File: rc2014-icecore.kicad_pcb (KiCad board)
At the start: 2 copper layers, 100 x 60.4 mm, 50 parts, among them J1 Conn_02x40_Top_Bottom, J2 Config, J3 DB15_Female_HighDensity_Mount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, P1 Mini-DIN_6pins_ver2, U1 SN74CB3T3245, U2 SN74CB3T3245, U3 SN74CB3T3245, U4 SN74CB3T3245, U5 SN74CB3T3245, U6 LM1117-3.3

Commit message: WIP
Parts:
- removed P1: Mini-DIN_6pins_ver2, 4x1md:Connector_Mini-DIN_Female_6Pin_2rows
- removed R1, R10, R11, R12, R16, R17, R18, R19, R2, R20, R24, R3, R4, R8, R9: 536, Resistor_SMD:R_0603_1608Metric
- removed R13, R14, R15, R21, R22, R23, R5, R6, R7: 270, Resistor_SMD:R_0603_1608Metric
- removed R25, R26: 100, Resistor_SMD:R_0603_1608Metric
- added J4: Conn_02x15_Odd_Even, Connector_PinSocket_2.54mm:PinSocket_2x15_P2.54mm_Horizontal, F.Cu at (128.3, 101.1)
- added J5: Conn_02x13_Odd_Even, Connector_PinHeader_2.54mm:PinHeader_2x13_P2.54mm_Horizontal, F.Cu at (266.1, 69.6)
- J3: value DB15_Female_HighDensity_MountingHoles -> Conn_02x15_Odd_Even; footprint Connector_Dsub:DSUB-15-HD_Female_Horizontal_P2.29x1.98mm_EdgePinOffset3.03mm_Housed_MountingHolesOffset4.94mm -> Connector_PinSocket_2.54mm:PinSocket_2x15_P2.54mm_Horizontal
- moved C11 24.7 mm to (127.1, 123.5)
- moved C7 24.7 mm to (123.3, 128.0)
- moved C6 24.7 mm to (127.3, 117.1)
- moved C12 24.7 mm to (131.4, 128.0)
- moved J3 16.8 mm to (140.9, 148.1), turned to 180 degrees
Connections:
- A1 pad 17: /VGA_R0 -> (no net)
- A1 pad 18: /VGA_R1 -> (no net)
- A1 pad 19: /VGA_R2 -> (no net)
- A1 pad 20: /VGA_G0 -> (no net)
- A1 pad 21: /VGA_G1 -> (no net)
- A1 pad 22: /VGA_G2 -> (no net)
- A1 pad 23: /VGA_B0 -> (no net)
- A1 pad 24: /VGA_B1 -> (no net)
- A1 pad 42: /VGA_HS -> (no net)
- A1 pad 43: /VGA_VS -> (no net)
- A1 pad 44: /VGA_B2 -> (no net)
- A1 pad 97: (no net) -> /RC_OE
- J2 pad 11: /DATA_OE -> (no net)
- J2 pad 13: /SIG_OE -> (no net)
- J2 pad 15: /SIG2_OE -> (no net)
- J2 pad 9: /ADDR_OE -> (no net)
- J3 pad 1: Net-(J3-Pad1) -> (no net)
- J3 pad 10: GND -> (no net)
- J3 pad 13: Net-(J3-Pad13) -> (no net)
- J3 pad 14: Net-(J3-Pad14) -> (no net)
- J3 pad 2: Net-(J3-Pad2) -> (no net)
- J3 pad 3: Net-(J3-Pad3) -> (no net)
- J3 pad 5: GND -> (no net)
- J3 pad 6: GND -> (no net)
- J3 pad 7: GND -> (no net)
- J3 pad 8: GND -> (no net)
- U1 pad 19: /ADDR_OE -> /RC_OE
- U2 pad 19: /ADDR_OE -> /RC_OE
- U3 pad 19: /SIG_OE -> /RC_OE
- U4 pad 19: /SIG2_OE -> /RC_OE
- U5 pad 19: /DATA_OE -> /RC_OE
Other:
- board size 100 x 60.4 mm -> 100.1 x 70.1 mm

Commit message: Board routed
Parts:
- removed C10, C11, C12, C8, C9: C, Capacitor_SMD:C_0603_1608Metric
- removed J2: Config, Connector_PinHeader_2.54mm:PinHeader_2x08_P2.54mm_Vertical
- removed J4: Conn_02x15_Odd_Even, Connector_PinSocket_2.54mm:PinSocket_2x15_P2.54mm_Horizontal
- moved J5 217.6 mm to (64.5, 151.6), turned to 180 degrees
- moved C2 77.8 mm to (149.5, 142.4)
- moved U6 77.8 mm to (143.1, 145.5)
- moved JP1 73.7 mm to (143.5, 129.7)
- moved C1 71.5 mm to (136.4, 142.2)
- moved C3 28.6 mm to (82.5, 120.4)
- moved C5 24.3 mm to (104.6, 120.4)
- moved C4 21.5 mm to (93.7, 120.4)
- moved J3 15.6 mm to (156.5, 147.3)
- moved U1 12.2 mm to (85.6, 127.5)
- moved U2 12.2 mm to (96.8, 127.5)
- moved U3 12.2 mm to (107.7, 127.5)
- moved U4 12.2 mm to (119.4, 127.5)
- moved U5 12.2 mm to (130.9, 127.5)
- moved C6 11.3 mm to (116.6, 120.7)
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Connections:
- A1 pad 1: /A14LV -> /P0
- A1 pad 10: /CLKLV -> /P17
- A1 pad 100: (no net) -> /P55
- A1 pad 11: /MREQLV -> /P20
- A1 pad 12: //RDLV -> /P21
- A1 pad 13: /D0LV -> /P24
- A1 pad 14: /D2LV -> /P25
- A1 pad 15: /D4LV -> /P28
- A1 pad 16: /D6LV -> /P29
- A1 pad 17: (no net) -> /P32
- A1 pad 18: (no net) -> /P33
- A1 pad 19: (no net) -> /P36
- A1 pad 2: /A12LV -> /P1
- A1 pad 20: (no net) -> /P37
- A1 pad 21: (no net) -> /P40
- A1 pad 22: (no net) -> /P41
- A1 pad 23: (no net) -> /P44
- A1 pad 24: (no net) -> /P45
- A1 pad 26: /A15LV -> /P2
- A1 pad 27: /A13LV -> /P3
- A1 pad 28: /A11LV -> /P6
- A1 pad 29: /A9LV -> /P7
- A1 pad 3: /A10LV -> /P4
- A1 pad 30: /A7LV -> /P10
- A1 pad 31: /A5LV -> /P11
- A1 pad 32: /A3LV -> /P14
- A1 pad 33: /A1LV -> /P15
- A1 pad 34: //RESETLV -> /P18
- A1 pad 35: /INTLV -> /P19
- A1 pad 36: //WRLV -> /P22
- A1 pad 37: //IORQLV -> /P23
- A1 pad 38: /D1LV -> /P26
- A1 pad 39: /D3LV -> /P27
- A1 pad 4: /A8LV -> /P5
- A1 pad 40: /D5LV -> /P30
- A1 pad 41: /D7LV -> /P31
- A1 pad 42: (no net) -> /P34
- A1 pad 43: (no net) -> /P35
- A1 pad 44: (no net) -> /P38
- A1 pad 45: (no net) -> /P39
- A1 pad 46: (no net) -> /P42
- A1 pad 47: (no net) -> /P43
- A1 pad 48: (no net) -> /P46
- A1 pad 49: (no net) -> /P47
- A1 pad 5: /A6LV -> /P8
- A1 pad 50: (no net) -> /FPGA_VCC
- A1 pad 52: (no net) -> /SWDIO
- A1 pad 53: (no net) -> /SWCLK
- A1 pad 54: (no net) -> /~RESET
- A1 pad 6: /A4LV -> /P9
- A1 pad 60: (no net) -> /AN5
- A1 pad 61: (no net) -> /AN6
- A1 pad 62: (no net) -> /AN7
- A1 pad 63: (no net) -> /AN8
- A1 pad 64: (no net) -> /AN9
- A1 pad 7: /A2LV -> /P12
- A1 pad 76: (no net) -> GND
- A1 pad 77: (no net) -> /~ESS
- A1 pad 78: (no net) -> /TX
- A1 pad 79: (no net) -> /RX
- A1 pad 8: /A0LV -> /P13
- A1 pad 80: (no net) -> /ESCK
- A1 pad 81: (no net) -> /EMISO
- A1 pad 82: (no net) -> /EMOSI
- A1 pad 83: (no net) -> /SCL
- A1 pad 84: (no net) -> /SDA
- A1 pad 85: (no net) -> /TMS
- A1 pad 86: (no net) -> /TDO
- A1 pad 87: (no net) -> /TDI
- A1 pad 88: (no net) -> /TCK
- A1 pad 89: (no net) -> +5V
- A1 pad 9: /M1LV -> /P16
- A1 pad 93: (no net) -> /P48
- A1 pad 94: (no net) -> /P49
- A1 pad 95: (no net) -> /P50
- A1 pad 96: (no net) -> /P51
- A1 pad 97: /RC_OE -> /P52
- A1 pad 98: (no net) -> /P53
- A1 pad 99: (no net) -> /P54
- J1 pad 33: (no net) -> GND
- J1 pad 38: (no net) -> /~RFSH
- J1 pad 44: (no net) -> /BUSACK
- J1 pad 46: (no net) -> /~HALT
- J1 pad 50: (no net) -> /~WAIT
- J1 pad 52: (no net) -> /~NMI
- J3 pad 1: (no net) -> +3V3
- J3 pad 10: (no net) -> /P36
- J3 pad 11: (no net) -> /P39
- J3 pad 12: (no net) -> /P37
- J3 pad 13: (no net) -> /AN9
- J3 pad 14: (no net) -> /AN8
- J3 pad 15: (no net) -> +5V
- J3 pad 16: (no net) -> /AN7
- J3 pad 17: (no net) -> /AN6
- J3 pad 18: (no net) -> /AN5
- J3 pad 19: (no net) -> +3V3
- J3 pad 2: (no net) -> +3V3
- J3 pad 20: (no net) -> +3V3
- J3 pad 21: (no net) -> GND
- J3 pad 22: (no net) -> GND
- J3 pad 23: (no net) -> /P42
- J3 pad 24: (no net) -> /P46
- J3 pad 25: (no net) -> /P43
- J3 pad 26: (no net) -> /P47
- J3 pad 27: (no net) -> /P40
- J3 pad 28: (no net) -> /P44
- J3 pad 29: (no net) -> /P41
- J3 pad 3: (no net) -> GND
- J3 pad 30: (no net) -> /P45
- J3 pad 4: (no net) -> GND
- J3 pad 5: (no net) -> /P34
- J3 pad 6: (no net) -> /P32
- J3 pad 7: (no net) -> /P35
- J3 pad 8: (no net) -> /P33
- J3 pad 9: (no net) -> /P38
- J5 pad 10: (no net) -> /TX
- J5 pad 11: (no net) -> /SWDIO
- J5 pad 12: (no net) -> /TCK
- J5 pad 13: (no net) -> /~RESET
- J5 pad 14: (no net) -> GND
- J5 pad 15: (no net) -> /TMS
- J5 pad 16: (no net) -> /TDI
- J5 pad 18: (no net) -> /TDO
- J5 pad 19: (no net) -> /EMOSI
- J5 pad 2: (no net) -> Net-(J5-Pad2)
- J5 pad 20: (no net) -> GND
- J5 pad 21: (no net) -> /EMISO
- J5 pad 23: (no net) -> /ESCK
- J5 pad 24: (no net) -> /~ESS
- J5 pad 25: (no net) -> GND
- J5 pad 3: (no net) -> /SDA
- J5 pad 4: (no net) -> Net-(J5-Pad2)
- J5 pad 5: (no net) -> /SCL
- J5 pad 6: (no net) -> GND
- J5 pad 7: (no net) -> /SWCLK
- J5 pad 8: (no net) -> /RX
- J5 pad 9: (no net) -> GND
- JP1 pad 3: (no net) -> /FPGA_VCC
- U1 pad 11: /A8LV -> /P8
- U1 pad 12: /A9LV -> /P6
- U1 pad 13: /A10LV -> /P5
- U1 pad 14: /A11LV -> /P3
- U1 pad 15: /A12LV -> /P4
- U1 pad 16: /A13LV -> /P2
- U1 pad 17: /A14LV -> /P1
- U1 pad 18: /A15LV -> /P0
- U1 pad 19: /RC_OE -> /P23
- U2 pad 11: /A0LV -> /P15
- U2 pad 12: /A1LV -> /P14
- U2 pad 13: /A2LV -> /P13
- U2 pad 14: /A3LV -> /P11
- U2 pad 15: /A4LV -> /P12
- U2 pad 16: /A5LV -> /P10
- U2 pad 17: /A6LV -> /P9
- U2 pad 18: /A7LV -> /P7
- U2 pad 19: /RC_OE -> /P23
- U3 pad 11: //IORQLV -> /P21
- U3 pad 12: //RDLV -> /P22
- U3 pad 13: //WRLV -> /P20
- U3 pad 14: /MREQLV -> /P19
- U3 pad 15: /M1LV -> /P17
- U3 pad 16: (no net) -> /P18
- U3 pad 17: (no net) -> /P16
- U3 pad 19: /RC_OE -> /P23
- U3 pad 4: (no net) -> /M1
- U3 pad 5: /M1 -> /~RFSH
- U3 pad 6: /MREQ -> //RESET
- U3 pad 7: //WR -> /CLK
- U3 pad 8: //RD -> /INT
- U3 pad 9: //IORQ -> /BUSACK
- U4 pad 11: /INTLV -> /P31
- U4 pad 12: /CLKLV -> /P29
- U4 pad 13: //RESETLV -> /P30
- U4 pad 14: (no net) -> /P28
- U4 pad 15: (no net) -> /P27
- U4 pad 16: (no net) -> /P25
- U4 pad 17: (no net) -> /P26
- U4 pad 18: (no net) -> /P24
- U4 pad 19: /RC_OE -> /P23
- U4 pad 2: (no net) -> /MREQ
- U4 pad 3: (no net) -> /~HALT
- U4 pad 4: (no net) -> //WR
- U4 pad 6: (no net) -> //RD
- U4 pad 7: //RESET -> /~WAIT
- U4 pad 8: /CLK -> //IORQ
- U4 pad 9: /INT -> /~NMI
- U5 pad 11: /D7LV -> /P55
- U5 pad 12: /D6LV -> /P54
- U5 pad 13: /D5LV -> /P53
- U5 pad 14: /D4LV -> /P52
- U5 pad 15: /D3LV -> /P51
- U5 pad 16: /D2LV -> /P50
- U5 pad 17: /D1LV -> /P49
- U5 pad 18: /D0LV -> /P48
- U5 pad 19: /RC_OE -> /P23
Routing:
- net GND: track 0.00 -> 191.8 mm, vias 0 -> 13
- net +3V3: track 0.00 -> 131.5 mm, vias 0 -> 6
- net +5V: track 0.00 -> 80.2 mm, vias 0 -> 2
- net /AN5: track 0.00 -> 74.7 mm, vias 0 -> 1
- net /P23: track 0.00 -> 70.2 mm
- net /AN6: track 0.00 -> 70.1 mm, vias 0 -> 1
- net /AN7: track 0.00 -> 66.7 mm, vias 0 -> 1
- net /P32: track 0.00 -> 64.5 mm
- net /AN8: track 0.00 -> 63.7 mm, vias 0 -> 2
- net /P33: track 0.00 -> 61.6 mm
- net /P36: track 0.00 -> 59.0 mm
- net /P34: track 0.00 -> 58.3 mm
- net /AN9: track 0.00 -> 56.8 mm, vias 0 -> 2
- net /P37: track 0.00 -> 56.7 mm
- net /TCK: track 0.00 -> 56.1 mm, vias 0 -> 1
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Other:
- board size 100.1 x 70.1 mm -> 100.1 x 63.3 mm
- net class Default: clearance 0.2 -> 0.1524
- net class gnd removed
- rule trace_clearance: 0.2 -> 0.1524
- board text added: "RC2014 IceCore Interface"
- board text removed: "RC2014 5V <-> 3.3V FPGA Interface"

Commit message: Board redesign
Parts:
- added J2: Conn_01x10, rc2014:PinHeader_1x10_P2.54mm_Vertical_NoSilk, F.Cu at (102.4, 160.8)
- J1: value Conn_02x40_Top_Bottom -> Conn_01x39; footprint Connector_PinHeader_2.54mm:PinHeader_2x39_P2.54mm_Vertical -> rc2014:PinHeader_1x39_P2.54mm_Vertical_NoSilk
- moved JP1 71.9 mm to (71.8, 124.6)
- moved C2 50.9 mm to (99.6, 132.2), turned to 180 degrees
- moved U1 43.4 mm to (100.3, 138.2)
- moved C1 41.3 mm to (95.6, 135.8), turned to 270 degrees
- moved J3 29.7 mm to (126.7, 146.6)
- moved C3 22.3 mm to (115.6, 139.2), turned to 270 degrees
- moved U6 17.5 mm to (120.5, 141.6)
- moved A1 8.52 mm to (84.7, 105.9)
- moved C7 6.70 mm to (110.7, 124.0), turned to 270 degrees
- moved C5 6.62 mm to (88.1, 124.0), turned to 270 degrees
- moved C4 6.41 mm to (77.2, 124.0), turned to 270 degrees
- moved C6 6.10 mm to (99.7, 124.0), turned to 270 degrees
- moved U5 4.10 mm to (115.6, 126.0)
- moved U3 3.87 mm to (93.2, 126.0)
- moved U2 3.64 mm to (82.3, 126.0)
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- renumbered C7 to C3, C3 to C4, C4 to C5, C5 to C6, C6 to C7, J5 to J4, U6 to U1, U1 to U2, U2 to U3, U3 to U4, U4 to U5, U5 to U6
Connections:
- J1 pad 10: (no net) -> /A6
- J1 pad 11: /A10 -> /A5
- J1 pad 12: (no net) -> /A4
- J1 pad 13: /A9 -> /A3
- J1 pad 14: (no net) -> /A2
- J1 pad 15: /A8 -> /A1
- J1 pad 16: (no net) -> /A0
- J1 pad 17: /A7 -> GND
- J1 pad 18: (no net) -> +5V
- J1 pad 19: /A6 -> /M1
- J1 pad 2: (no net) -> /A14
- J1 pad 20: (no net) -> //RESET
- J1 pad 21: /A5 -> /CLK
- J1 pad 22: (no net) -> /INT
- J1 pad 23: /A4 -> /MREQ
- J1 pad 24: (no net) -> //WR
- J1 pad 25: /A3 -> //RD
- J1 pad 26: (no net) -> //IORQ
- J1 pad 27: /A2 -> /D0
- J1 pad 28: (no net) -> /D1
- J1 pad 29: /A1 -> /D2
- J1 pad 3: /A14 -> /A13
- J1 pad 30: (no net) -> /D3
- J1 pad 31: /A0 -> /D4
- J1 pad 32: (no net) -> /D5
- J1 pad 33: GND -> /D6
- J1 pad 34: GND -> /D7
- J1 pad 35: +5V -> (no net)
- J1 pad 36: +5V -> (no net)
- J1 pad 37: /M1 -> (no net)
- J1 pad 38: /~RFSH -> (no net)
- J1 pad 39: //RESET -> (no net)
- J1 pad 4: (no net) -> /A12
- J1 pad 5: /A13 -> /A11
- J1 pad 6: (no net) -> /A10
- J1 pad 7: /A12 -> /A9
- J1 pad 8: (no net) -> /A8
- J1 pad 9: /A11 -> /A7
- J3 pad 24: /P46 -> /P43
- J3 pad 25: /P43 -> /P46
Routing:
- net GND: track 191.8 -> 246.3 mm, vias 13 -> 0
- net +3V3: track 131.5 -> 184.7 mm, vias 6 -> 1
- net /P46: track 48.7 -> 17.5 mm
- net /AN6: track 70.1 -> 40.0 mm
- net /AN5: track 74.7 -> 45.4 mm
- net Net-(C2-Pad1): track 27.0 -> 55.2 mm, vias 0 -> 1
- net /AN8: track 63.7 -> 37.8 mm, vias 2 -> 1
- net /AN7: track 66.7 -> 41.2 mm
- net /P45: track 41.4 -> 18.1 mm
- net /AN9: track 56.8 -> 34.3 mm, vias 2 -> 1
- net /P44: track 43.2 -> 21.5 mm
- net /P40: track 42.2 -> 20.5 mm
- net /P41: track 39.9 -> 18.2 mm
- net /P42: track 42.9 -> 21.3 mm, vias 0 -> 1
- net /P47: track 40.4 -> 18.9 mm
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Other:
- board size 100.1 x 63.3 mm -> 99.3 x 60.1 mm
- board text added: "CLK/NC"
- board text added: "INT/BUSACK"
- board text added: "IORQ/NMI"
- board text added: "M1/RFSH"
- board text added: "MRQ/HALT"
- board text added: "RD/WAIT"
- board text added: "RST/NC"
- board text added: "WR/NC"
- board text removed: "CLK"
- board text removed: "INT"
- board text removed: "IORQ"
- board text removed: "M1"
- board text removed: "MRQ"
- board text removed: "RD"
- board text removed: "RST"
- board text removed: "WR"

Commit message: 2nd redesign
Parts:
- added R1: R, Resistor_SMD:R_0603_1608Metric, F.Cu at (79.1, 119.9)
- moved C2 6.52 mm to (105.0, 135.8), turned to 270 degrees
- moved C1 0.13 mm to (95.8, 135.8)
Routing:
- net GND: track 246.3 -> 257.3 mm
- net /P23: track 75.7 -> 80.7 mm
- net +3V3: track 184.7 -> 188.6 mm
- net Net-(C2-Pad1): track 55.2 -> 57.8 mm
- net /M1: track 36.9 -> 39.0 mm
- net /~RFSH: track 33.5 -> 35.5 mm
- net //RESET: track 36.6 -> 38.5 mm
- net /~NMI: track 38.0 -> 38.7 mm
- net /D0: track 22.8 -> 23.5 mm
- net /P49: track 21.4 -> 20.7 mm
- net /D3: track 25.2 -> 25.9 mm
- net /D2: track 24.4 -> 25.1 mm
- net /D1: track 23.6 -> 24.3 mm
- net /P50: track 20.8 -> 20.1 mm
- net //IORQ: track 40.8 -> 41.3 mm
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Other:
- net class Power added: clearance 0.1524, trace_width 0.381, via_dia 0.6858, via_drill 0.3302
- net class vcc removed

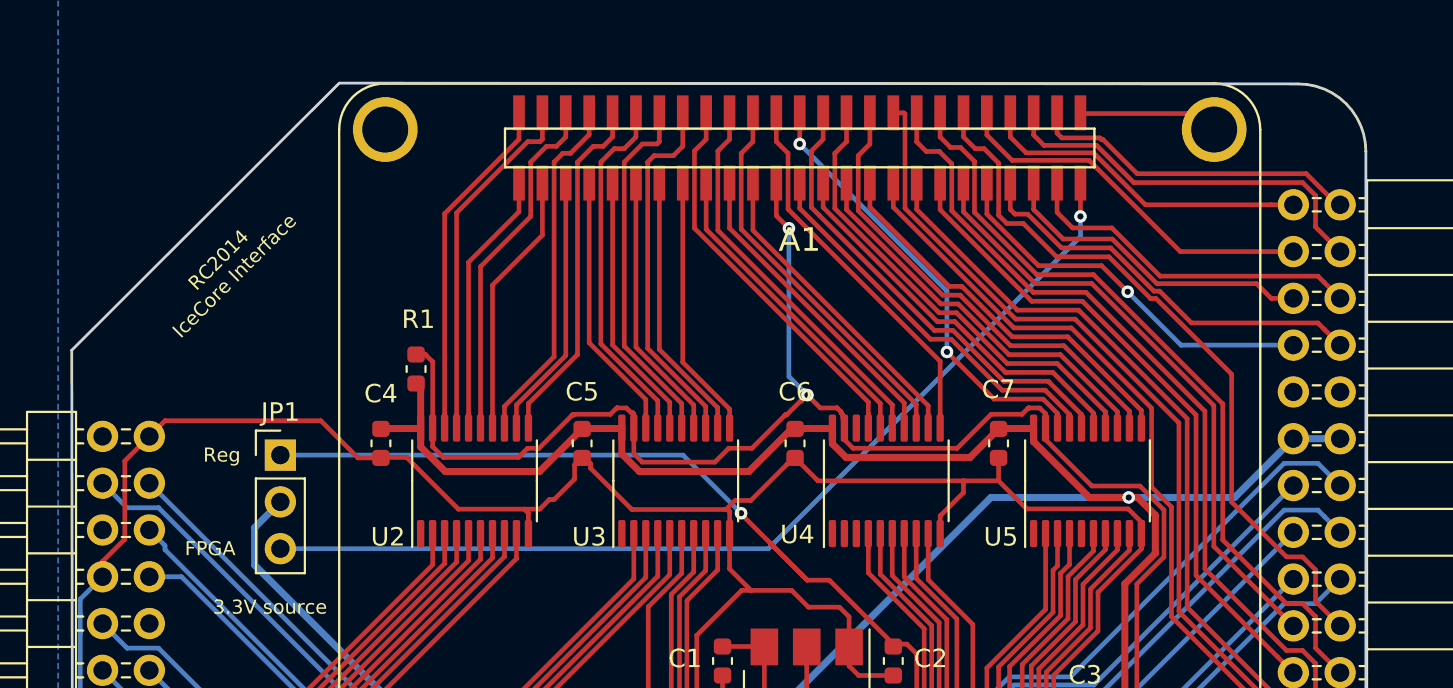
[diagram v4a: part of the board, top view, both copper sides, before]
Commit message: reorder pmod pins
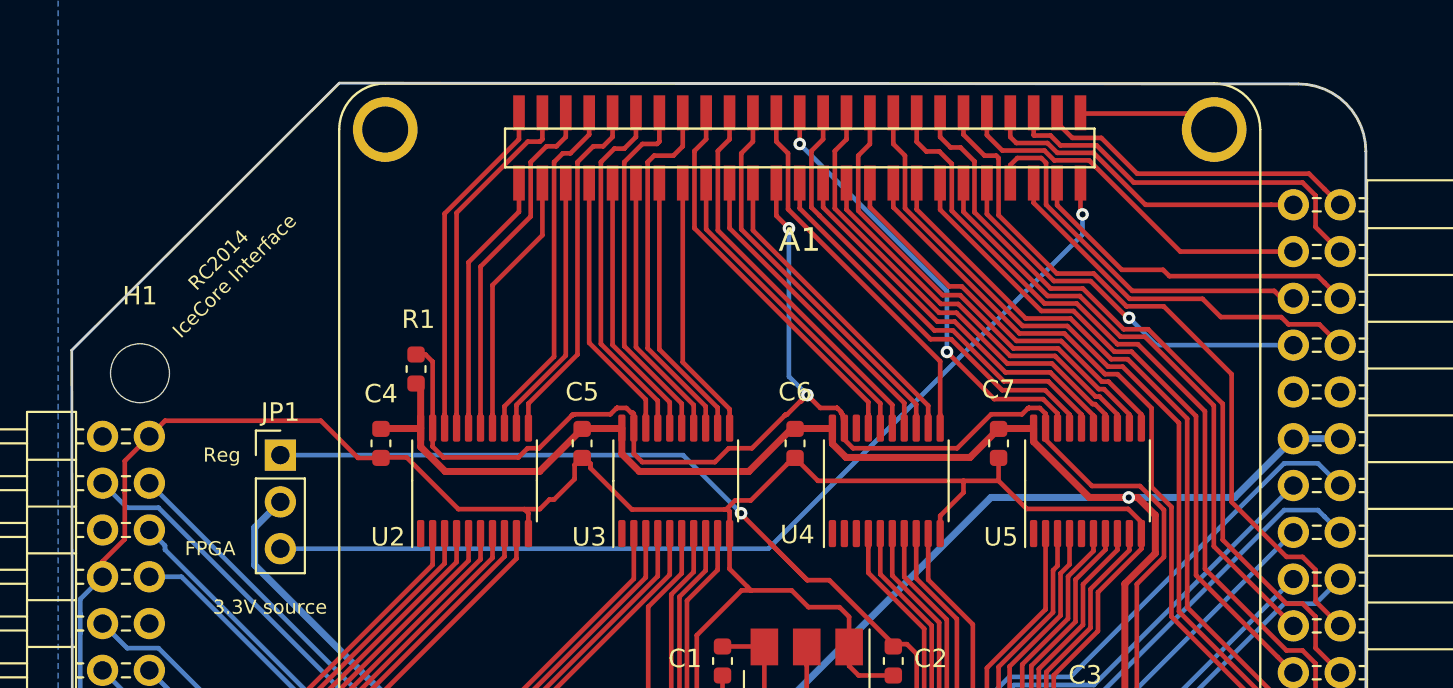
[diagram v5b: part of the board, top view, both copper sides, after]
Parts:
- added H1: MountingHole, MountingHole:MountingHole_3.2mm_M3, F.Cu at (64.1, 120.1)
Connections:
- J3 pad 24: /P43 -> /P46
- J3 pad 25: /P46 -> /P43
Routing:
- net /P46: track 17.5 -> 20.9 mm
- net /P43: track 22.4 -> 21.0 mm

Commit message: WIP
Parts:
- removed C1: 100nF, Capacitor_SMD:C_0603_1608Metric
- removed C2: 10uF, Capacitor_SMD:C_0603_1608Metric
- removed C3, C4, C5, C6, C7: C, Capacitor_SMD:C_0603_1608Metric
- removed H1: MountingHole, MountingHole:MountingHole_3.2mm_M3
- removed J4: Conn_02x13_Odd_Even, Connector_PinHeader_2.54mm:PinHeader_2x13_P2.54mm_Horizontal
- removed JP1: Ext Power, Connector_PinHeader_2.54mm:PinHeader_1x03_P2.54mm_Vertical
- removed R1: R, Resistor_SMD:R_0603_1608Metric
- removed U1: LM1117-3.3, Package_TO_SOT_SMD:SOT-223-3_TabPin2
- removed U2, U3, U4, U5, U6: SN74CB3T3245, Package_SO:TSSOP-20_4.4x6.5mm_P0.65mm
- J1: value Conn_01x39 -> Conn_02x25_Odd_Even; footprint rc2014:PinHeader_1x39_P2.54mm_Vertical_NoSilk -> Connector_PinHeader_2.54mm:PinHeader_2x25_P2.54mm_Vertical
- J2: value Conn_01x10 -> Conn_02x15_Odd_Even; footprint rc2014:PinHeader_1x10_P2.54mm_Vertical_NoSilk -> Connector_PinSocket_2.54mm:PinSocket_2x15_P2.54mm_Vertical
- J3: value Conn_02x15_Odd_Even -> Conn_02x13_Odd_Even; footprint Connector_PinSocket_2.54mm:PinSocket_2x15_P2.54mm_Horizontal -> Connector_PinHeader_2.54mm:PinHeader_2x13_P2.54mm_Vertical
- moved J3 62.5 mm to (64.6, 154.0)
- moved J2 27.1 mm to (126.7, 148.8), turned to 180 degrees
- moved J1 4.32 mm to (65.5, 161.3)
- moved A1 0.46 mm to (84.3, 106.2)
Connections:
- J1 pad 1: /A15 -> /P0
- J1 pad 10: /A6 -> /P9
- J1 pad 11: /A5 -> /P10
- J1 pad 12: /A4 -> /P11
- J1 pad 13: /A3 -> /P12
- J1 pad 14: /A2 -> /P13
- J1 pad 15: /A1 -> /P14
- J1 pad 16: /A0 -> /P15
- J1 pad 17: GND -> /P16
- J1 pad 18: +5V -> /P17
- J1 pad 19: /M1 -> /P18
- J1 pad 2: /A14 -> /P1
- J1 pad 20: //RESET -> /P19
- J1 pad 21: /CLK -> /P20
- J1 pad 22: /INT -> /P21
- J1 pad 23: /MREQ -> /P22
- J1 pad 24: //WR -> /P23
- J1 pad 25: //RD -> /P24
- J1 pad 26: //IORQ -> /P25
- J1 pad 27: /D0 -> /P26
- J1 pad 28: /D1 -> /P27
- J1 pad 29: /D2 -> /P28
- J1 pad 3: /A13 -> /P2
- J1 pad 30: /D3 -> /P29
- J1 pad 31: /D4 -> /P30
- J1 pad 32: /D5 -> /P31
- J1 pad 33: /D6 -> /P48
- J1 pad 34: /D7 -> /P49
- J1 pad 35: (no net) -> /P50
- J1 pad 36: (no net) -> /P51
- J1 pad 37: (no net) -> /P52
- J1 pad 38: (no net) -> /P53
- J1 pad 39: (no net) -> /P54
- J1 pad 4: /A12 -> /P3
- J1 pad 5: /A11 -> /P4
- J1 pad 6: /A10 -> /P5
- J1 pad 7: /A9 -> /P6
- J1 pad 8: /A8 -> /P7
- J1 pad 9: /A7 -> /P8
- J2 pad 1: GND -> /FPGA_VCC
- J2 pad 10: /~NMI -> /P36
- J2 pad 2: +5V -> /FPGA_VCC
- J2 pad 3: /~RFSH -> GND
- J2 pad 4: (no net) -> GND
- J2 pad 5: (no net) -> /P34
- J2 pad 6: /BUSACK -> /P32
- J2 pad 7: /~HALT -> /P35
- J2 pad 8: (no net) -> /P33
- J2 pad 9: /~WAIT -> /P38
- J3 pad 1: +3V3 -> (no net)
- J3 pad 10: /P36 -> /TX
- J3 pad 11: /P39 -> /SWDIO
- J3 pad 12: /P37 -> /TCK
- J3 pad 13: /AN9 -> /~RESET
- J3 pad 14: /AN8 -> GND
- J3 pad 15: +5V -> /TMS
- J3 pad 16: /AN7 -> /TDI
- J3 pad 17: /AN6 -> (no net)
- J3 pad 18: /AN5 -> /TDO
- J3 pad 19: +3V3 -> /EMOSI
- J3 pad 2: +3V3 -> Net-(J3-Pad2)
- J3 pad 20: +3V3 -> GND
- J3 pad 21: GND -> /EMISO
- J3 pad 22: GND -> (no net)
- J3 pad 23: /P42 -> /ESCK
- J3 pad 24: /P46 -> /~ESS
- J3 pad 25: /P43 -> GND
- J3 pad 26: /P47 -> (no net)
- J3 pad 3: GND -> /SDA
- J3 pad 4: GND -> Net-(J3-Pad2)
- J3 pad 5: /P34 -> /SCL
- J3 pad 6: /P32 -> GND
- J3 pad 7: /P35 -> /SWCLK
- J3 pad 8: /P33 -> /RX
- J3 pad 9: /P38 -> GND
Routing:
- net +3V3: track 188.6 -> 0.00 mm, vias 1 -> 0
- net /P24: track 24.5 -> 98.7 mm, vias 2 -> 0
- net /P9: track 19.5 -> 91.3 mm
- net GND: track 257.3 -> 187.6 mm, vias 0 -> 3
- net Net-(C2-Pad1): track 57.8 -> 0.00 mm, vias 1 -> 0
- net /A4: track 50.6 -> 0.00 mm
- net /A5: track 48.6 -> 0.00 mm
- net /P2: track 14.4 -> 62.6 mm
- net /P17: track 21.3 -> 68.7 mm
- net /P14: track 14.6 -> 61.4 mm
- net /A6: track 46.6 -> 0.00 mm
- net /P0: track 18.8 -> 64.8 mm
- net /A7: track 44.8 -> 0.00 mm
- net /P12: track 19.7 -> 64.5 mm
- net /P10: track 14.6 -> 59.4 mm
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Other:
- board size 99.3 x 60.1 mm -> 70.3 x 60.7 mm
- board text added: "github.com/electrified/rc2014-icecore"
- board text removed: "+5V"
- board text removed: "3.3V source"
- board text removed: "A0"
- board text removed: "A1"
- board text removed: "A10"
- board text removed: "A11"
- board text removed: "A12"
- board text removed: "A13"
- board text removed: "A14"
- board text removed: "A15"
- board text removed: "A2"
- board text removed: "A3"
- board text removed: "A4"
- board text removed: "A5"
- board text removed: "A6"
- board text removed: "A7"
- board text removed: "A8"
- board text removed: "A9"
- board text removed: "CLK/NC"
- board text removed: "D0"
- board text removed: "D1"
- board text removed: "D2"
- board text removed: "D3"
- board text removed: "D4"
- board text removed: "D5"
- board text removed: "D6"
- board text removed: "D7"
- board text removed: "FPGA"
- board text removed: "GND"
- board text removed: "INT/BUSACK"
- board text removed: "IORQ/NMI"
- board text removed: "M1/RFSH"
- board text removed: "MRQ/HALT"
- board text removed: "RD/WAIT"
- board text removed: "RST/NC"
- board text removed: "Reg"
- board text removed: "WR/NC"
- board text removed: "github.com/electrified/rc2014-fpga-interface"

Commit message: Rev 1 as sent to JLCPCB
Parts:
- added G***: LOGO, rc2014:blackedge, F.Cu at (67.9, 115.3)
- added G***: LOGO, rc2014:maxreal, B.Cu at (101.8, 126.2)
- added REF**: OSHW-Symbol_6.7x6mm_SilkScreen, Symbol:OSHW-Symbol_6.7x6mm_SilkScreen, B.Cu at (116.3, 141.5)
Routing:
- net /P27: track 55.9 -> 53.5 mm
- net /P26: track 58.1 -> 55.8 mm
- net /P29: track 56.7 -> 54.7 mm
- net /P21: track 56.5 -> 55.5 mm
- net /P28: track 57.5 -> 56.6 mm
- net /AN5: track 44.6 -> 43.8 mm
- net /P22: track 54.8 -> 54.0 mm
- net /P24: track 98.7 -> 98.0 mm
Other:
- board text added: "2020 Ed Brindley"
- board text added: "github.com/electrified/rc2014-blackedge"
- board text removed: "2018, 2020 Ed Brindley"
- board text removed: "RC2014 IceCore Interface"
- board text removed: "github.com/electrified/rc2014-icecore"
